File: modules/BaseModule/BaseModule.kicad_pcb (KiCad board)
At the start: 2 copper layers, 85 x 60 mm, 58 parts, among them J1 Conn_01x04, J10 Conn_01x02_Male, J11 DB9_Female_MountingHoles, J12 Conn_01x02_Male, J13 Conn_01x02_Male, J2 Conn_01x02_Male, J3 Conn_01x04, J4 Conn_02x03_Odd_Even, J5 Conn_01x15_Male, J6 proto_grid_15x21, J7 Conn_02x02_Top_Bottom, J8 Conn_02x02_Top_Bottom, J9 Conn_01x02_Male, SW1 SW_Push, U1 STM32F103C8, U2 LM1117-5.0, U3 LM1117-3.3, U4 MAX485E, U5 MAX485E, Y1 8 MHz, Y2 32.768 KHz

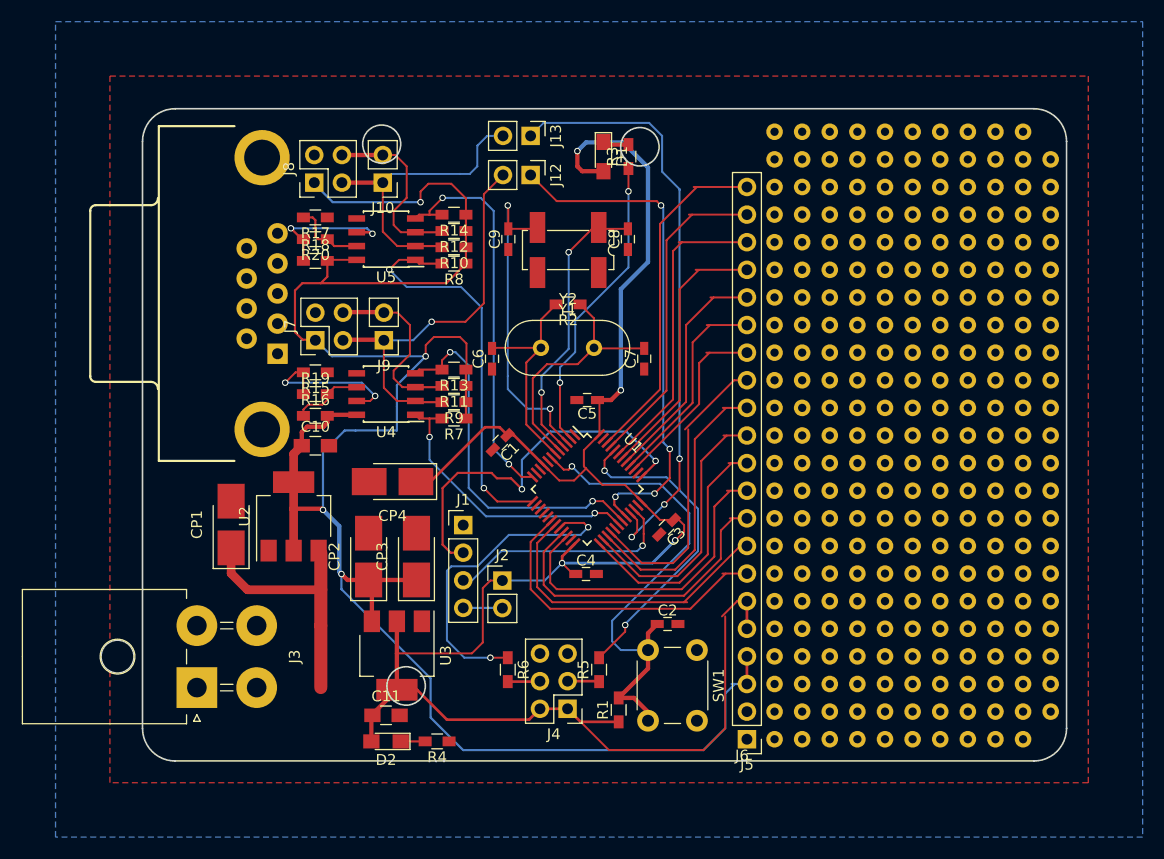
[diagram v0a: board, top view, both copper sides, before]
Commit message: BaseModule updates and documentation updates
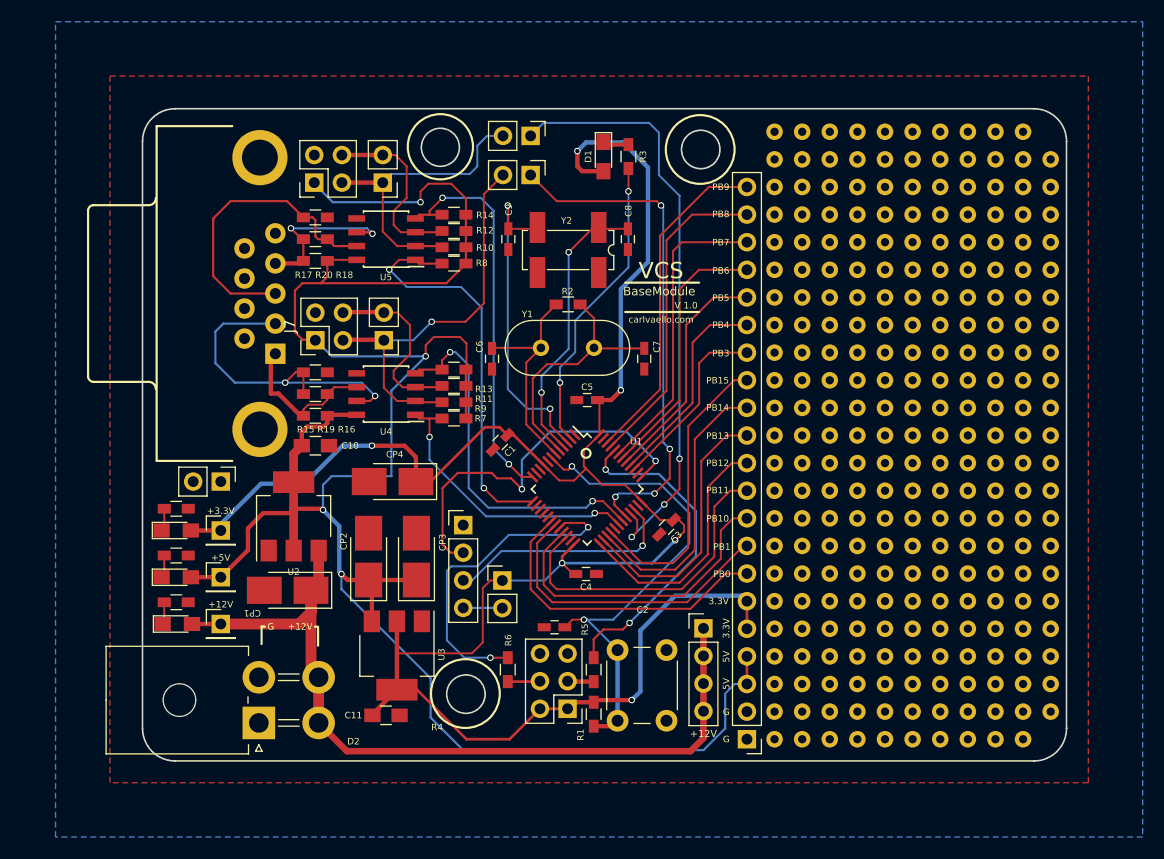
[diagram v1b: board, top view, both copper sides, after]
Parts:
- added D3: LED, LEDs:LED_0805_HandSoldering, F.Cu at (3.10, 43.1)
- added D4: LED, LEDs:LED_0805_HandSoldering, F.Cu at (3.20, 47.4)
- added J14: Conn_01x01, Pin_Headers:Pin_Header_Straight_1x01_Pitch2.54mm, F.Cu at (7.20, 38.8)
- added J15: Conn_01x01, Pin_Headers:Pin_Header_Straight_1x01_Pitch2.54mm, F.Cu at (7.20, 43.1)
- added J16: Conn_01x01, Pin_Headers:Pin_Header_Straight_1x01_Pitch2.54mm, F.Cu at (7.20, 47.4)
- added J17: Conn_01x02_Top_Bottom, Pin_Headers:Pin_Header_Straight_1x02_Pitch2.54mm, F.Cu at (7.20, 34.3)
- added J18: Conn_02x02_Top_Bottom, Socket_Strips:Socket_Strip_Straight_1x04_Pitch2.54mm, F.Cu at (51.6, 47.8)
- added R21: 510R, Resistors_SMD:R_0603_HandSoldering, F.Cu at (3.10, 41.1)
- added R22: 510R, Resistors_SMD:R_0603_HandSoldering, F.Cu at (3.10, 45.4)
- C10, C11: value 0.1uF -> 100nF
- C2: value 105 -> 1.0uF
- J11: value DB9_Female_MountingHoles -> DB9_Female
- J3: footprint Connectors_Molex:Molex_MegaFit_2x02x5.70mm_Angled -> Connectors_Molex:Molex_MiniFit-JR-5569-04A2_2x02x4.20mm_Angled
- moved R4 32.2 mm to (3.10, 36.8)
- moved D2 27.4 mm to (3.10, 38.8), turned to 0 degrees
- moved C2 10.4 mm to (37.9, 47.7), turned to 180 degrees
- moved CP1 7.98 mm to (13.3, 44.3), turned to 180 degrees
- moved J3 6.56 mm to (10.7, 56.5)
- moved SW1 2.80 mm to (48.2, 49.8)
- moved R1 2.33 mm to (41.5, 55.7), turned to 270 degrees
- moved R5 0.50 mm to (41.5, 51.6)
- moved J11 0.20 mm to (10.8, 17.0)
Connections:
- J11 pad 1: I_A -> O_A
- J11 pad 2: Net-(J11-Pad2) -> O_B
- J11 pad 3: Net-(J11-Pad3) -> I_B
- J11 pad 4: Net-(J11-Pad4) -> I_A
- J11 pad 5: Net-(J11-Pad5) -> GND
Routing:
- net +12V: track 23.9 -> 77.2 mm
- net I_B: track 6.87 -> 28.1 mm
- net O_B: track 14.7 -> 30.6 mm
- net +3V3: track 180.2 -> 195.3 mm, vias 4 -> 6
- net +5V: track 185.9 -> 199.1 mm
- net O_A: track 6.64 -> 14.3 mm
- net I_A: track 12.8 -> 15.3 mm
- net Net-(D3-Pad1): track 0.00 -> 2.10 mm
- net Net-(D4-Pad1): track 0.00 -> 2.06 mm
- net PB9: track 31.8 -> 30.9 mm
- net BOOT0: track 29.8 -> 30.5 mm
- net Net-(J4-Pad3): track 2.92 -> 2.42 mm
- net RESET: track 46.1 -> 45.9 mm, vias 1 -> 2
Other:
- outline, holes or cut-outs redrawn
- board text added: "+12V"
- board text added: "+3.3V"
- board text added: "+5V"
- board text added: "3.3V"
- board text added: "5V"
- board text added: "BaseModule"
- board text added: "C1"
- board text added: "C10"
- board text added: "C11"
- board text added: "C2"
- board text added: "C3"
- board text added: "C4"
- board text added: "C5"
- board text added: "C6"
- board text added: "C7"
- board text added: "C8"
- board text added: "C9"
- board text added: "CP1"
- board text added: "CP2"
- board text added: "CP3"
- board text added: "CP4"
- board text added: "D1"
- board text added: "D2"
- board text added: "G"
- board text added: "PB0"
- board text added: "PB1"
- board text added: "PB10"
- board text added: "PB11"
- board text added: "PB12"
- board text added: "PB13"
- board text added: "PB14"
- board text added: "PB15"
- board text added: "PB3"
- board text added: "PB4"
- board text added: "PB5"
- board text added: "PB6"
- board text added: "PB7"
- board text added: "PB8"
- board text added: "PB9"
- board text added: "R1"
- board text added: "R10"
- board text added: "R11"
- board text added: "R12"
- board text added: "R13"
- board text added: "R14"
- board text added: "R15 R19 R16"
- board text added: "R17 R20 R18"
- board text added: "R2"
- board text added: "R3"
- board text added: "R4"
- board text added: "R5"
- board text added: "R6"
- board text added: "R7"
- board text added: "R8"
- board text added: "R9"
- board text added: "U1"
- board text added: "U2"
- board text added: "U3"
- board text added: "U4"
- board text added: "U5"
- board text added: "V 1.0"
- board text added: "VCS"
- board text added: "Y1"
- board text added: "Y2"
- board text added: "carlvaello.com"
